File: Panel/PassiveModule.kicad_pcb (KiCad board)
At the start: 2 copper layers, 25 x 200 mm, 12 parts

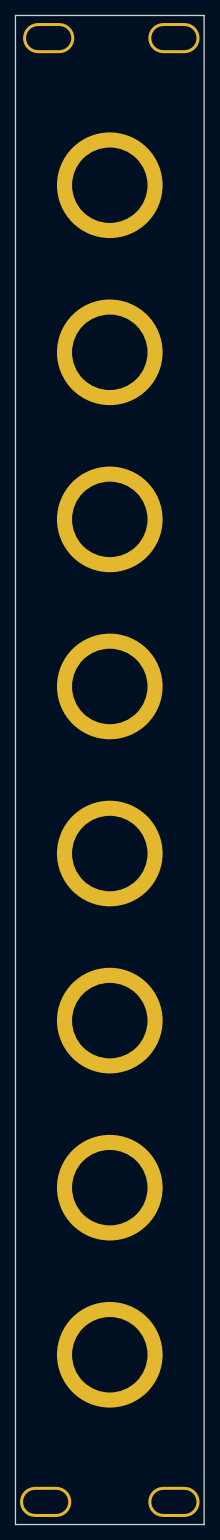
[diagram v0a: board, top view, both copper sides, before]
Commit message: add silkscreen
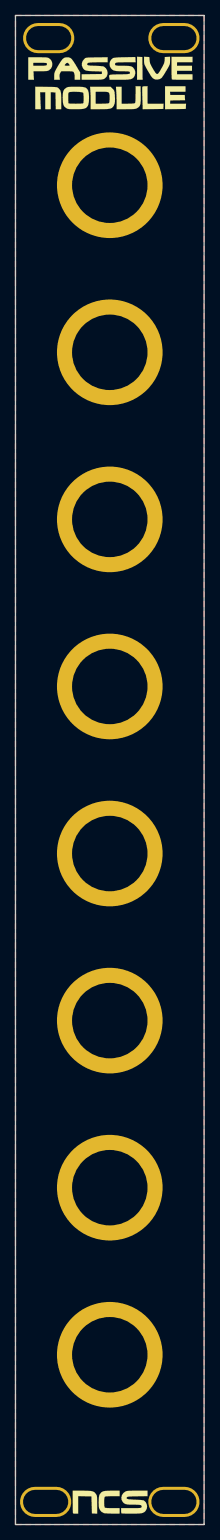
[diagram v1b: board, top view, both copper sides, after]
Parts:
- added G***: LOGO, PassiveModule:silkscreen, F.Cu at (1.50, 100.0)
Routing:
- added copper zone on F.Cu, net GND
